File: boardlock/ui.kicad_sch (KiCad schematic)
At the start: 34 parts, among them Q5 MMBT4401, Q6 MMBT4401, Q7 MMBT4401, SW1 SW_Push, SW2 SW_Push

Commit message: continuing to add footprints
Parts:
- C?: footprint (none) -> Capacitor_SMD:C_0805_2012Metric_Pad1.18x1.45mm_HandSolder
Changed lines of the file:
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@@
       (effects (font (size 1.27 1.27)) (justify left))
     )
-    (property "Footprint" "" (at 91.1352 54.61 0)
+    (property "Footprint" "Capacitor_SMD:C_0805_2012Metric_Pad1.18x1.45mm_HandSolder" (at 91.1352 54.61 0)
       (effects (font (size 1.27 1.27)) hide)
     )

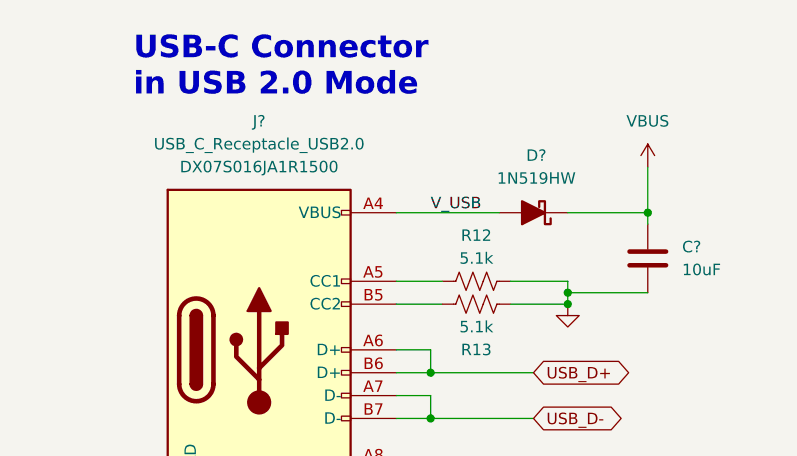
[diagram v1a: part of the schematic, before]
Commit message: footprint updates
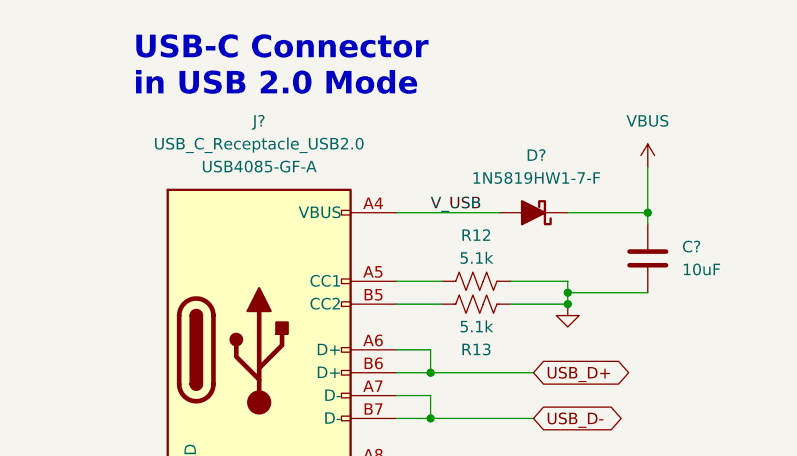
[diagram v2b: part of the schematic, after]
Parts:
- D?: value 1N519HW -> 1N5819HW1-7-F; MF (none) -> Diodes Incorporated
- J?: footprint Connector_USB:USB_C_Receptacle_JAE_DX07S016JA1R1500 -> Connector_USB:USB_C_Receptacle_GCT_USB4085; MFN Part # DX07S016JA1R1500 -> USB4085-GF-A
- U?: footprint Package_TO_SOT_SMD:SOT-543 -> Package_TO_SOT_SMD:SOT-553
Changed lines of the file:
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@@
       (effects (font (size 1.27 1.27)))
     )
-    (property "Footprint" "Package_TO_SOT_SMD:SOT-543" (at 123.19 72.39 0)
+    (property "Footprint" "Package_TO_SOT_SMD:SOT-553" (at 123.19 72.39 0)
       (effects (font (size 1.27 1.27)) hide)
     )
@@
       (effects (font (size 1.27 1.27)))
     )
-    (property "Value" "1N519HW" (at 77.7875 41.91 0)
+    (property "Value" "1N5819HW1-7-F" (at 77.7875 41.91 0)
       (effects (font (size 1.27 1.27)))
     )
@@
     )
     (property "Datasheet" "~" (at 77.47 45.72 0)
+      (effects (font (size 1.27 1.27)) hide)
+    )
+    (property "MF" "Diodes Incorporated" (at 77.47 45.72 0)
       (effects (font (size 1.27 1.27)) hide)
     )
@@
       (effects (font (size 1.27 1.27)))
     )
-    (property "Footprint" "Connector_USB:USB_C_Receptacle_JAE_DX07S016JA1R1500" (at 50.8 27.94 0)
-      (effects (font (size 1.27 1.27)) hide)
-    )
-    (property "Datasheet" "https://www.digikey.com/en/products/detail/jae-electronics/dx07s016ja1r1500/11585731" (at 50.8 30.48 0)
-      (effects (font (size 1.27 1.27)) hide)
-    )
-    (property "MFN Part #" "DX07S016JA1R1500" (at 46.99 40.64 0)
-      (effects (font (size 1.27 1.27)))
-    )
+    (property "Footprint" "Connector_USB:USB_C_Receptacle_GCT_USB4085" (at 50.8 27.94 0)
+      (effects (font (size 1.27 1.27)) hide)
+    )
+    (property "Datasheet" "https://www.digikey.com/en/products/detail/gct/USB4085-GF-A/9859662" (at 50.8 30.48 0)
+      (effects (font (size 1.27 1.27)) hide)
+    )
+    (property "MFN Part #" "USB4085-GF-A" (at 46.99 40.64 0)
+      (effects (font (size 1.27 1.27)))
+    )

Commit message: more footprint selection
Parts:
- R39: footprint (none) -> Resistor_SMD:R_0805_2012Metric_Pad1.20x1.40mm_HandSolder
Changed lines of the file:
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@@
       (effects (font (size 1.27 1.27)) (justify left))
     )
-    (property "Footprint" "" (at 44.196 164.084 90)
+    (property "Footprint" "Resistor_SMD:R_0805_2012Metric_Pad1.20x1.40mm_HandSolder" (at 44.196 164.084 90)
       (effects (font (size 1.27 1.27)) hide)
     )

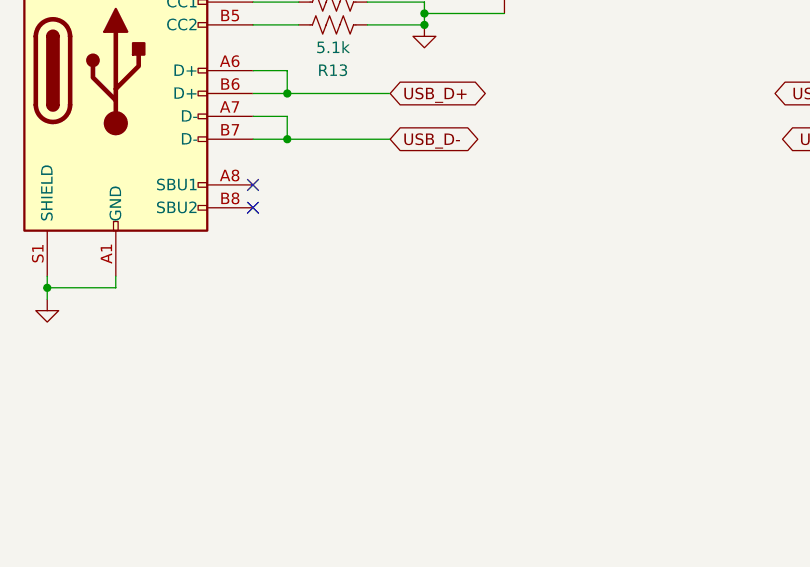
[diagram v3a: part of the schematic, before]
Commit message: added buzzer power circuit
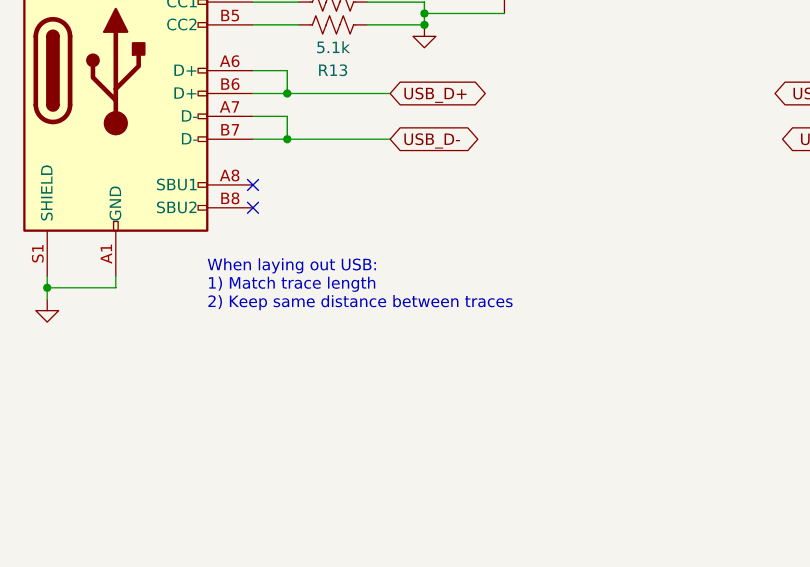
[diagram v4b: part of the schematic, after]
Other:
- note added: "When laying out USB: 1) Match trace length 2) Keep same distance between traces"
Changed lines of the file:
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@@
+    (effects (font (size 1.27 1.27)) (justify left bottom))
+  )
+  (text "When laying out USB:\n1) Match trace length\n2) Keep same distance between traces"
+    (at 57.15 87.63 0)
     (effects (font (size 1.27 1.27)) (justify left bottom))
   )

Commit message: footprint work
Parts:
- C23, C24: footprint (none) -> Capacitor_SMD:C_0805_2012Metric_Pad1.18x1.45mm_HandSolder
- D2: footprint (none) -> LED_SMD:LED_Cree-PLCC4_3.2x2.8mm_CCW
- Q5, Q6, Q7: footprint (none) -> Package_TO_SOT_SMD:SOT-23-3
- SW1, SW2: footprint (none) -> Button_Switch_SMD:SW_Push_1P1T_NO_Vertical_Wuerth_434133025816
- gave numbers to parts that had none: 4
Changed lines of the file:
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@@
   (symbol (lib_id "Power_Protection:TPD2E2U06") (at 143.51 66.04 0) (unit 1)
     (in_bom yes) (on_board yes) (dnp no) (fields_autoplaced)
-    (property "Reference" "U?" (at 143.51 55.88 0)
+    (property "Reference" "U9" (at 143.51 55.88 0)
       (effects (font (size 1.27 1.27)))
     )
@@
       (project "boardlock"
         (path "/e1fc29ce-837e-4062-84d8-c7e423f9eab9/c1e95beb-a482-4f8e-b13b-3641abb17f9b"
-          (reference "U?") (unit 1)
+          (reference "U9") (unit 1)
         )
       )
@@
       (effects (font (size 1.27 1.27)) (justify right))
     )
-    (property "Footprint" "" (at 99.06 138.43 0)
+    (property "Footprint" "LED_SMD:LED_Cree-PLCC4_3.2x2.8mm_CCW" (at 99.06 138.43 0)
       (effects (font (size 1.27 1.27)) hide)
     )
@@
       (effects (font (size 1.27 1.27)))
     )
-    (property "Footprint" "" (at 234.95 44.45 0)
+    (property "Footprint" "Capacitor_SMD:C_0805_2012Metric_Pad1.18x1.45mm_HandSolder" (at 234.95 44.45 0)
       (effects (font (size 1.27 1.27)) hide)
     )
@@
       (effects (font (size 1.27 1.27)))
     )
-    (property "Footprint" "" (at 259.08 91.44 0)
+    (property "Footprint" "Capacitor_SMD:C_0805_2012Metric_Pad1.18x1.45mm_HandSolder" (at 259.08 91.44 0)
       (effects (font (size 1.27 1.27)) hide)
     )
@@
       (effects (font (size 1.27 1.27)))
     )
-    (property "Footprint" "" (at 227.33 35.56 0)
+    (property "Footprint" "Button_Switch_SMD:SW_Push_1P1T_NO_Vertical_Wuerth_434133025816" (at 227.33 35.56 0)
       (effects (font (size 1.27 1.27)) hide)
     )
@@
       (effects (font (size 1.27 1.27)))
     )
-    (property "Footprint" "" (at 214.63 113.03 0)
+    (property "Footprint" "Capacitor_SMD:C_0805_2012Metric_Pad1.18x1.45mm_HandSolder" (at 214.63 113.03 0)
       (effects (font (size 1.27 1.27)) hide)
     )
@@
       (effects (font (size 1.27 1.27)) (justify left))
     )
-    (property "Footprint" "" (at 158.75 158.75 0)
+    (property "Footprint" "Package_TO_SOT_SMD:SOT-23-3" (at 158.75 158.75 0)
       (effects (font (size 1.27 1.27)) hide)
     )
@@
       (effects (font (size 1.27 1.27)) (justify left))
     )
-    (property "Footprint" "" (at 113.03 158.75 0)
+    (property "Footprint" "Package_TO_SOT_SMD:SOT-23-3" (at 113.03 158.75 0)
       (effects (font (size 1.27 1.27)) hide)
     )
@@
       (effects (font (size 1.27 1.27)))
     )
-    (property "Footprint" "" (at 200.66 44.45 0)
+    (property "Footprint" "Capacitor_SMD:C_0805_2012Metric_Pad1.18x1.45mm_HandSolder" (at 200.66 44.45 0)
       (effects (font (size 1.27 1.27)) hide)
     )
@@
       (effects (font (size 1.27 1.27)))
     )
-    (property "Footprint" "" (at 214.63 91.44 0)
+    (property "Footprint" "Capacitor_SMD:C_0805_2012Metric_Pad1.18x1.45mm_HandSolder" (at 214.63 91.44 0)
       (effects (font (size 1.27 1.27)) hide)
     )
@@
   (symbol (lib_id "Device:C") (at 90.17 50.8 0) (unit 1)
     (in_bom yes) (on_board yes) (dnp no) (fields_autoplaced)
-    (property "Reference" "C?" (at 93.98 49.53 0)
+    (property "Reference" "C34" (at 93.98 49.53 0)
       (effects (font (size 1.27 1.27)) (justify left))
     )
@@
       (project "boardlock"
         (path "/e1fc29ce-837e-4062-84d8-c7e423f9eab9/c1e95beb-a482-4f8e-b13b-3641abb17f9b"
-          (reference "C?") (unit 1)
+          (reference "C34") (unit 1)
         )
       )
@@
       (effects (font (size 1.27 1.27)))
     )
-    (property "Footprint" "" (at 243.84 82.55 0)
+    (property "Footprint" "Button_Switch_SMD:SW_Push_1P1T_NO_Vertical_Wuerth_434133025816" (at 243.84 82.55 0)
       (effects (font (size 1.27 1.27)) hide)
     )
@@
       (effects (font (size 1.27 1.27)))
     )
-    (property "Footprint" "" (at 193.04 35.56 0)
+    (property "Footprint" "Button_Switch_SMD:SW_Push_1P1T_NO_Vertical_Wuerth_434133025816" (at 193.04 35.56 0)
       (effects (font (size 1.27 1.27)) hide)
     )
@@
       (effects (font (size 1.27 1.27)) (justify left))
     )
-    (property "Footprint" "" (at 203.2 160.02 0)
+    (property "Footprint" "Package_TO_SOT_SMD:SOT-23-3" (at 203.2 160.02 0)
       (effects (font (size 1.27 1.27)) hide)
     )
@@
   (symbol (lib_id "Device:D_Schottky_Filled") (at 77.47 45.72 180) (unit 1)
     (in_bom yes) (on_board yes) (dnp no) (fields_autoplaced)
-    (property "Reference" "D?" (at 77.7875 39.37 0)
+    (property "Reference" "D2" (at 77.7875 39.37 0)
       (effects (font (size 1.27 1.27)))
     )
@@
       (project "boardlock"
         (path "/e1fc29ce-837e-4062-84d8-c7e423f9eab9/c1e95beb-a482-4f8e-b13b-3641abb17f9b"
-          (reference "D?") (unit 1)
+          (reference "D2") (unit 1)
         )
       )
@@
   (symbol (lib_id "Connector:USB_C_Receptacle_USB2.0") (at 46.99 60.96 0) (unit 1)
     (in_bom yes) (on_board yes) (dnp no)
-    (property "Reference" "J?" (at 46.99 35.56 0)
+    (property "Reference" "J6" (at 46.99 35.56 0)
       (effects (font (size 1.27 1.27)))
     )
@@
       (project "boardlock"
         (path "/e1fc29ce-837e-4062-84d8-c7e423f9eab9/c1e95beb-a482-4f8e-b13b-3641abb17f9b"
-          (reference "J?") (unit 1)
-        )
-      )
+          (reference "J6") (unit 1)
+        )
+      )

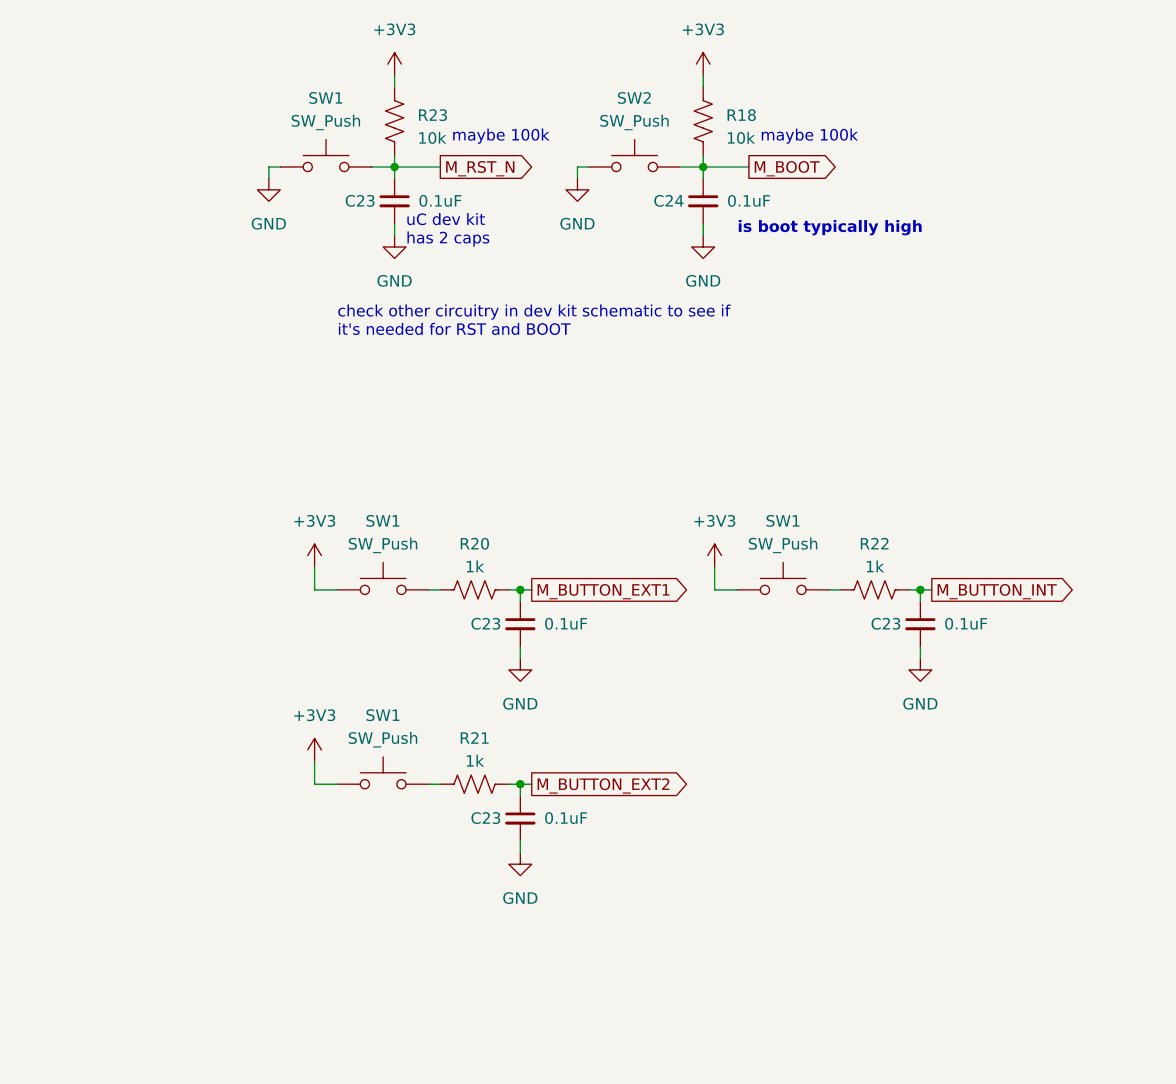
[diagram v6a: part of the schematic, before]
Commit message: correcting old schematic and footprints
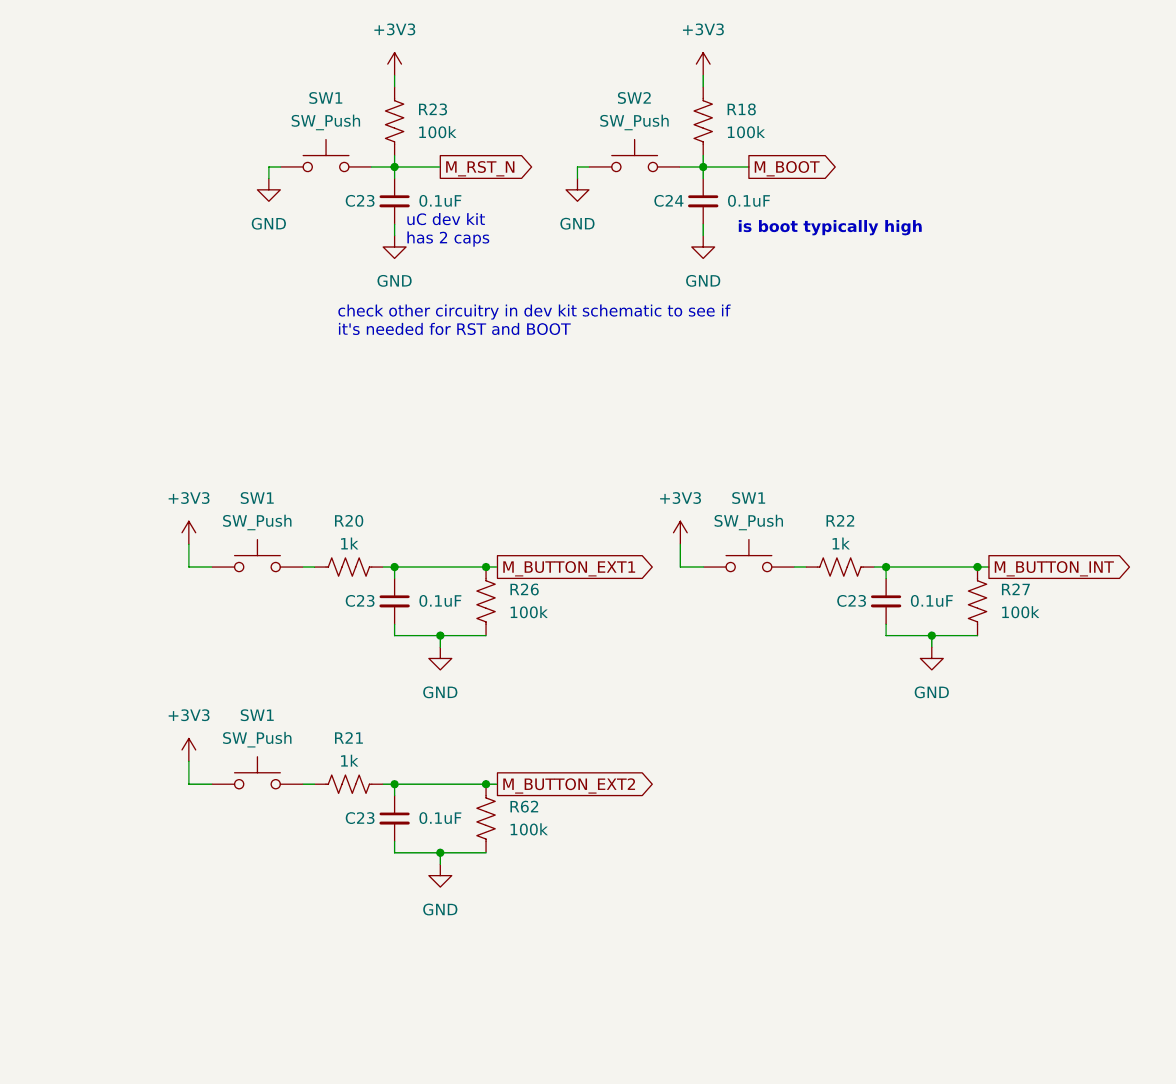
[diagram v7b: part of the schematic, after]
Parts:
- added R26, R27, R62: 100k, Resistor_SMD:R_0805_2012Metric_Pad1.20x1.40mm_HandSolder, symbol Device:R_US
- R18, R23: value 10k -> 100k
- SW1: footprint (none) -> TL3300DF160Q:SW_TL3300DF160Q
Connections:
- net GND: now also R26.1, R27.1, R62.1
- net M_BUTTON_EXT1: now also R26.2
- net M_BUTTON_EXT2: now also R62.2
- net M_BUTTON_INT: now also R27.2
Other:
- note removed: "maybe 100k"
- moved on the sheet: C23, R20, R21, R22, SW1

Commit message: more pcb stuff
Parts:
- renumbered C34 to C31, D2 to D3, R23 to R41, R18 to R42, R12 to R43, R13 to R44, R20 to R45, R22 to R46, R26 to R47, R27 to R48, R21 to R49, R62 to R50, R31 to R51, R34 to R52, R37 to R53, R32 to R54, R33 to R55, R36 to R56, R39 to R57, R30 to R58, R35 to R59
